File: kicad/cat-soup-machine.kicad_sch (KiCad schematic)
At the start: 6 parts, among them M1 FEEDER MOTOR, M2 PUMP, Q1 TIP120

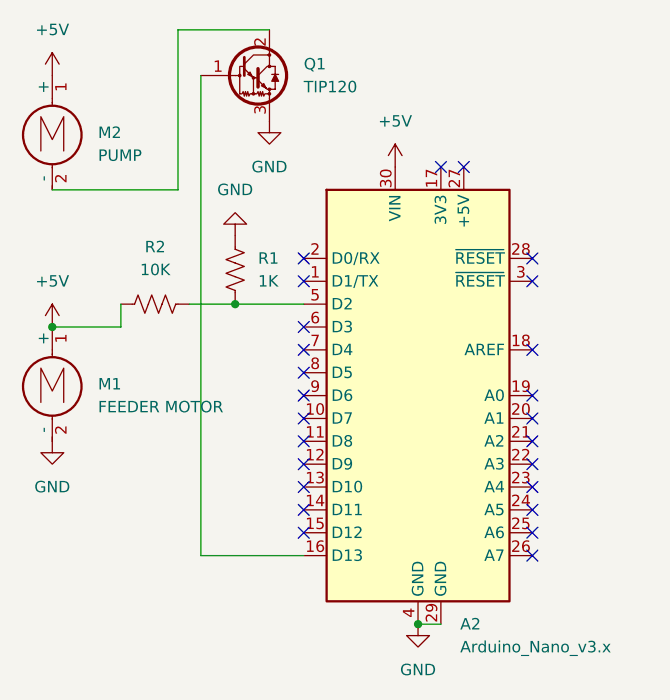
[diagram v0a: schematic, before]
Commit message: update running time
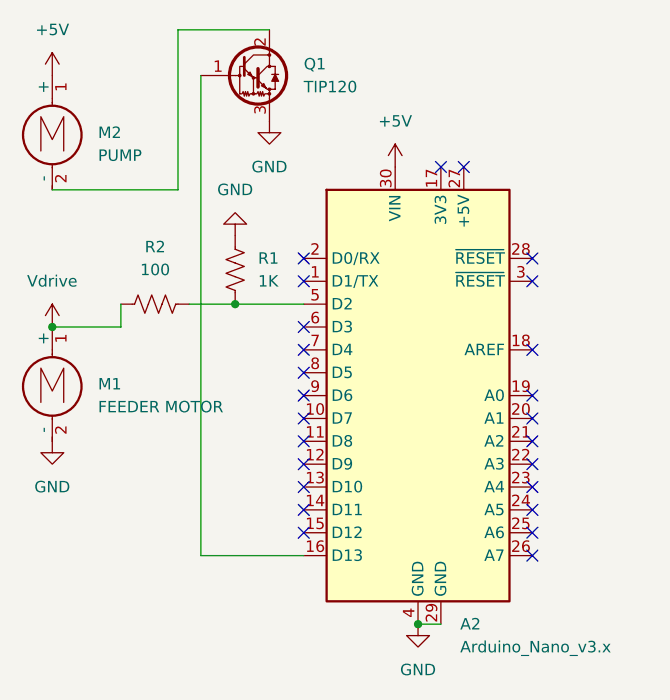
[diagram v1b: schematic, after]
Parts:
- R2: value 10K -> 100
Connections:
- net +5V: no longer M1.1 (+), R2.1
- new net Vdrive: M1.1 (+), R2.1
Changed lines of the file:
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@@
+	)
+	(symbol
+		(lib_id "power:Vdrive")
+		(at 113.03 58.42 0)
+		(unit 1)
+		(exclude_from_sim no)
+		(in_bom yes)
+		(on_board yes)
+		(dnp no)
+		(property "Reference" "#PWR08"
+			(at 113.03 62.23 0)
+			(effects
+				(font
+					(size 1.27 1.27)
+				)
+				(hide yes)
+			)
+		)
+		(property "Value" "Vdrive"
+			(at 113.03 53.34 0)
+			(effects
+				(font
+					(size 1.27 1.27)
+				)
+			)
+		)
+		(property "Footprint" ""
+			(at 113.03 58.42 0)
+			(effects
+				(font
+					(size 1.27 1.27)
+				)
+				(hide yes)
+			)
+		)
+		(property "Datasheet" ""
+			(at 113.03 58.42 0)
+			(effects
+				(font
+					(size 1.27 1.27)
+				)
+				(hide yes)
+			)
+		)
+		(property "Description" "Power symbol creates a global label with name \"Vdrive\""
+			(at 113.03 58.42 0)
+			(effects
+				(font
+					(size 1.27 1.27)
+				)
+				(hide yes)
+			)
+		)
+		(pin "1"
+		)
+		(instances
+			(project ""
+				(path "/4dad4d1e-688d-417b-8ab1-47b2780f69f2"
+					(reference "#PWR08")
+					(unit 1)
+				)
+			)
+		)
 	)
 	(symbol
@@
 	)
 	(symbol
+		(lib_id "power:GND")
+		(at 113.03 71.12 0)
+		(unit 1)
+		(exclude_from_sim no)
+		(in_bom yes)
+		(on_board yes)
+		(dnp no)
+		(fields_autoplaced yes)
+		(property "Reference" "#PWR03"
+			(at 113.03 77.47 0)
+			(effects
+				(font
+					(size 1.27 1.27)
+				)
+				(hide yes)
+			)
+		)
+		(property "Value" "GND"
+			(at 113.03 76.2 0)
+			(effects
+				(font
+					(size 1.27 1.27)
+				)
+			)
+		)
+		(property "Footprint" ""
+			(at 113.03 71.12 0)
+			(effects
+				(font
+					(size 1.27 1.27)
+				)
+				(hide yes)
+			)
+		)
+		(property "Datasheet" ""
+			(at 113.03 71.12 0)
+			(effects
+				(font
+					(size 1.27 1.27)
+				)
+				(hide yes)
+			)
+		)
+		(property "Description" "Power symbol creates a global label with name \"GND\" , ground"
+			(at 113.03 71.12 0)
+			(effects
+				(font
+					(size 1.27 1.27)
+				)
+				(hide yes)
+			)
+		)
+		(pin "1"
+		)
+		(instances
+			(project ""
+				(path "/4dad4d1e-688d-417b-8ab1-47b2780f69f2"
+					(reference "#PWR03")
+					(unit 1)
+				)
+			)
+		)
+	)
+	(symbol
 		(lib_id "Motor:Motor_DC")
 		(at 113.03 63.5 0)
@@
 			)
 		)
-		(property "Value" "10K"
+		(property "Value" "100"
 			(at 124.46 52.07 90)
 			(effects
@@
 	)
 	(symbol
-		(lib_id "power:GND")
-		(at 113.03 71.12 0)
-		(unit 1)
-		(exclude_from_sim no)
-		(in_bom yes)
-		(on_board yes)
-		(dnp no)
-		(fields_autoplaced yes)
-		(property "Reference" "#PWR03"
-			(at 113.03 77.47 0)
-			(effects
-				(font
-					(size 1.27 1.27)
-				)
-				(hide yes)
-			)
-		)
-		(property "Value" "GND"
-			(at 113.03 76.2 0)
-			(effects
-				(font
-					(size 1.27 1.27)
-				)
-			)
-		)
-		(property "Footprint" ""
-			(at 113.03 71.12 0)
-			(effects
-				(font
-					(size 1.27 1.27)
-				)
-				(hide yes)
-			)
-		)
-		(property "Datasheet" ""
-			(at 113.03 71.12 0)
-			(effects
-				(font
-					(size 1.27 1.27)
-				)
-				(hide yes)
-			)
-		)
-		(property "Description" "Power symbol creates a global label with name \"GND\" , ground"
-			(at 113.03 71.12 0)
-			(effects
-				(font
-					(size 1.27 1.27)
-				)
-				(hide yes)
-			)
-		)
-		(pin "1"
-		)
-		(instances
-			(project ""
-				(path "/4dad4d1e-688d-417b-8ab1-47b2780f69f2"
-					(reference "#PWR03")
-					(unit 1)
-				)
-			)
-		)
-	)
-	(symbol
 		(lib_id "MCU_Module:Arduino_Nano_v3.x")
 		(at 153.67 66.04 0)
@@
 					(unit 1)
 				)
-			)
-		)
-	)
-	(symbol
-		(lib_id "power:+5V")
-		(at 113.03 58.42 0)
-		(unit 1)
-		(exclude_from_sim no)
-		(in_bom yes)
-		(on_board yes)
-		(dnp no)
-		(fields_autoplaced yes)
-		(property "Reference" "#PWR04"
-			(at 113.03 62.23 0)
-			(effects
-				(font
-					(size 1.27 1.27)
-				)
-				(hide yes)
-			)
-		)
-		(property "Value" "+5V"
-			(at 113.03 53.34 0)
-			(effects
-				(font
-					(size 1.27 1.27)
-				)
-			)
-		)
-		(property "Footprint" ""
-			(at 113.03 58.42 0)
-			(effects
-				(font
-					(size 1.27 1.27)
-				)
-				(hide yes)
-			)
-		)
-		(property "Datasheet" ""
-			(at 113.03 58.42 0)
-			(effects
-				(font
-					(size 1.27 1.27)
-				)
-				(hide yes)
-			)
-		)
-		(property "Description" "Power symbol creates a global label with name \"+5V\""
-			(at 113.03 58.42 0)
-			(effects
-				(font
-					(size 1.27 1.27)
-				)
-				(hide yes)
-			)
-		)
-		(pin "1"
-		)
-		(instances
-			(project ""
-				(path "/4dad4d1e-688d-417b-8ab1-47b2780f69f2"
-					(reference "#PWR04")
-					(unit 1)
-				)
